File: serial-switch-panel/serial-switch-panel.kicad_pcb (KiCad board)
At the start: 2 copper layers, 59 parts, among them J10 Conn_01x01, J11 Conn_01x01, J12 Conn_01x01, J13 Conn_01x01, J14 Conn_01x01, J15 Conn_01x01, J16 Conn_01x01, J17 Conn_01x01, J18 Conn_01x01, J2 2501551-4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

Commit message: Final? front-panel placement
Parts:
- moved R1 17.8 mm to (138.1, 97.2), turned to 180 degrees
- moved J13 11.7 mm to (112.7, 87.1)
- moved C6 11.0 mm to (129.1, 100.6)
- moved U1 11.0 mm to (129.5, 97.5)
- moved J3 10.8 mm to (138.1, 87.1)
- moved J4 10.8 mm to (135.6, 87.1)
- moved J5 10.8 mm to (133.0, 87.1)
- moved J7 10.8 mm to (127.9, 87.1)
- moved J8 10.8 mm to (125.4, 87.1)
- moved J9 10.8 mm to (122.9, 87.1)
- moved J10 10.8 mm to (120.3, 87.1)
- moved J6 10.8 mm to (130.5, 87.1)
- moved R12 10.8 mm to (138.1, 93.4)
- moved R13 10.8 mm to (135.6, 93.4)
- moved R15 10.8 mm to (133.0, 93.4)
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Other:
- board outline added: 41.9 x 31.8 mm

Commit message: [fp] Correct P4+/- swap in ethernet connector
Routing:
- net /CLK_N: track 0.00 -> 6.39 mm
- net /CLK_P: track 0.00 -> 5.92 mm
- net GND: track 0.00 -> 5.73 mm, vias 0 -> 3
- net Net-(J9-Pin_1): track 0.00 -> 2.48 mm
- net Net-(J8-Pin_1): track 0.00 -> 2.48 mm
- net Net-(J7-Pin_1): track 0.00 -> 2.48 mm
- net Net-(J6-Pin_1): track 0.00 -> 2.48 mm
- net Net-(J5-Pin_1): track 0.00 -> 2.48 mm
- net Net-(J4-Pin_1): track 0.00 -> 2.48 mm
- net Net-(J3-Pin_1): track 0.00 -> 2.48 mm
- net Net-(J10-Pin_1): track 0.00 -> 2.48 mm
- net +5V: track 0.00 -> 1.94 mm
- net /IN_H: track 0.00 -> 1.40 mm
- net /IN_G: track 0.00 -> 1.40 mm
- net /IN_F: track 0.00 -> 1.40 mm
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- added copper zone on B.Cu, net GND

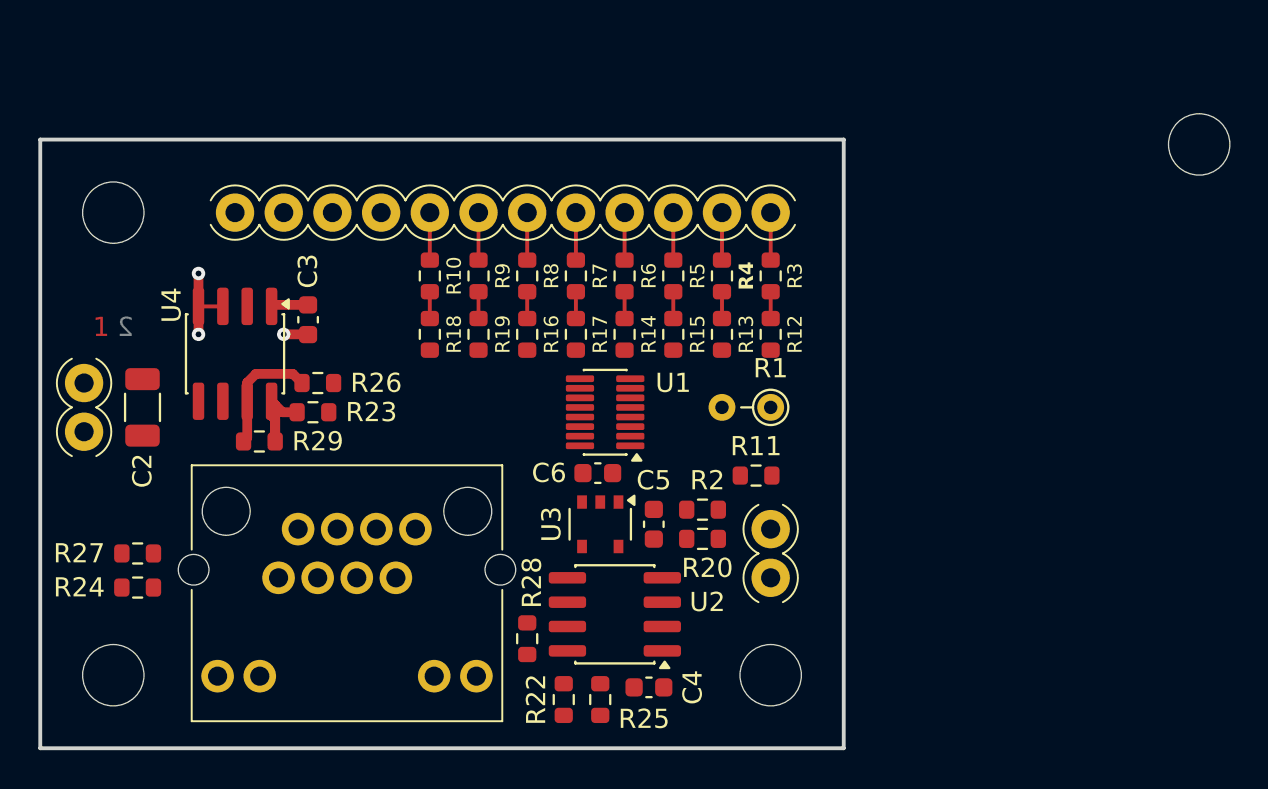
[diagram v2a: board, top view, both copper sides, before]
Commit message: [fp] Complete board route
Note: lots of DRC errors & warnings.
- Warnings are silk overlaps - these are fine
- Most errors are clearance violations on the shift register - waving these as still > 6mil
- Remaining errors are thermal spokes on non-critical components & fill regions
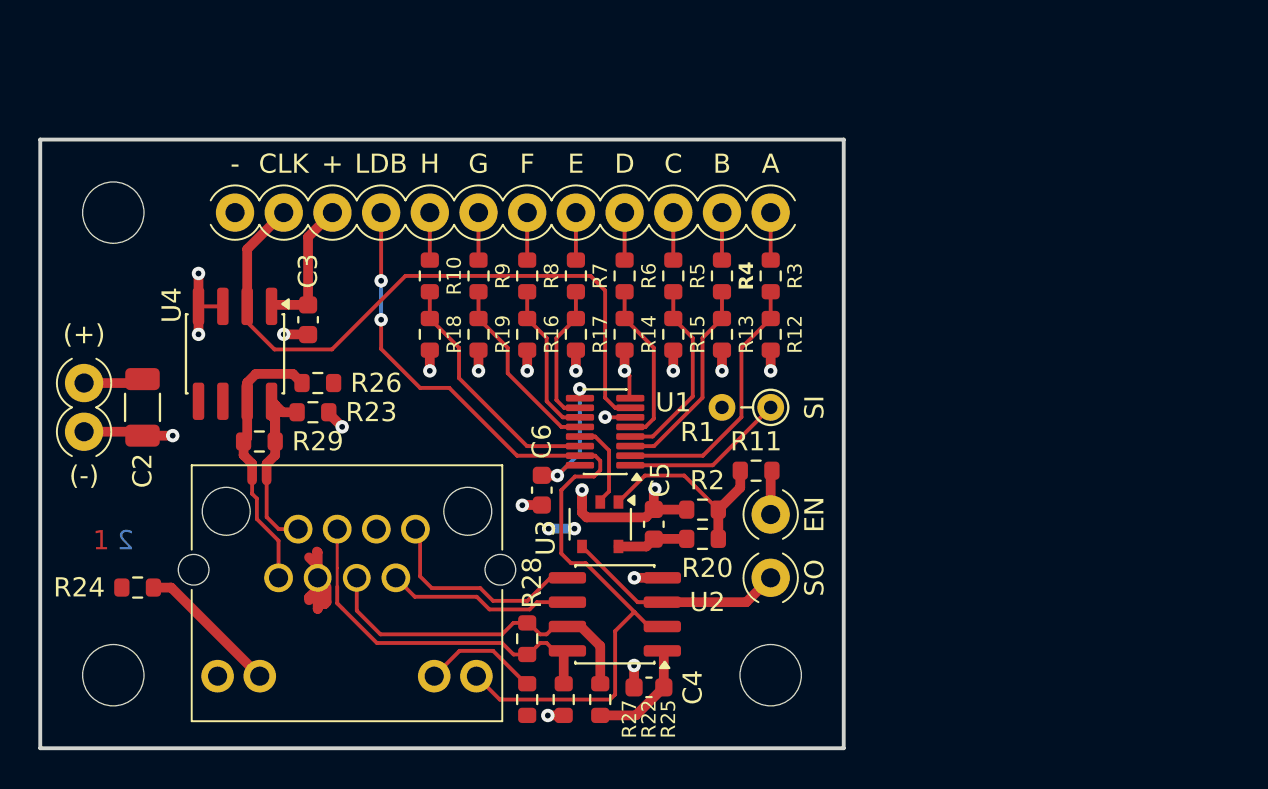
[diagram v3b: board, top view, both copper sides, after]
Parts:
- removed the H1 at (160.5, 83.5)
- moved R27 21.7 mm to (125.4, 112.5), turned to -90 degrees
- moved LAY1 11.1 mm to (103.2, 105.4)
- moved C6 3.05 mm to (126.2, 101.5), turned to -90 degrees
- moved J13 2.54 mm to (115.2, 87.1)
- moved J18 2.54 mm to (112.7, 87.1)
- moved U1 1.02 mm to (129.5, 98.5)
- moved J11 0.76 mm to (138.1, 102.8)
- moved R11 0.25 mm to (137.3, 100.5)
- renumbered H2 to H1, H3 to H2, H4 to H3
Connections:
- J2 pad 1: /CLK_P -> /CLK_N
- J2 pad 2: /CLK_N -> /CLK_P
- J2 pad 4: /LD_N -> /LD_P
- J2 pad 5: /LD_P -> /LD_N
- U3 pad 1: Net-(U1-Qh) -> Net-(R11-Pad2)
- U3 pad 2: Net-(R11-Pad2) -> Net-(U1-Qh)
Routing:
- net /LOADB: track 0.00 -> 46.6 mm, vias 0 -> 2
- net +5V: track 1.94 -> 38.0 mm, vias 0 -> 4
- net /CLK: track 0.00 -> 34.8 mm
- net GND: track 5.73 -> 35.5 mm, vias 3 -> 20
- net /LD_P: track 0.00 -> 19.2 mm
- net /LD_N: track 0.00 -> 18.0 mm
- net /IN_A: track 1.40 -> 13.8 mm
- net /IN_H: track 1.40 -> 13.1 mm
- net /SCAN_OUT: track 0.00 -> 11.6 mm
- net /SO_P: track 0.00 -> 11.3 mm
- net Net-(R11-Pad2): track 0.00 -> 10.5 mm
- net /SO_N: track 0.00 -> 9.79 mm
- net /IN_B: track 1.40 -> 10.8 mm
- net /IN_C: track 1.40 -> 10.0 mm
- net /SCAN_IN: track 0.00 -> 8.57 mm
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- added copper zone on F.Cu, net +5V
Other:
- board text added: "(+)"
- board text added: "(-)"
- board text added: "+"
- board text added: "-"
- board text added: "A"
- board text added: "B"
- board text added: "C"
- board text added: "CLK"
- board text added: "D"
- board text added: "E"
- board text added: "EN"
- board text added: "F"
- board text added: "G"
- board text added: "H"
- board text added: "LDB"
- board text added: "SI"
- board text added: "SO"
